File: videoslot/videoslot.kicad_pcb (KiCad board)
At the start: 2 copper layers, 100 x 24 mm, 11 parts, among them CN203 CN451/203, CN207 CN452/207, P1 VA2000, U1 74LVC8T245, U2 74LVC8T245

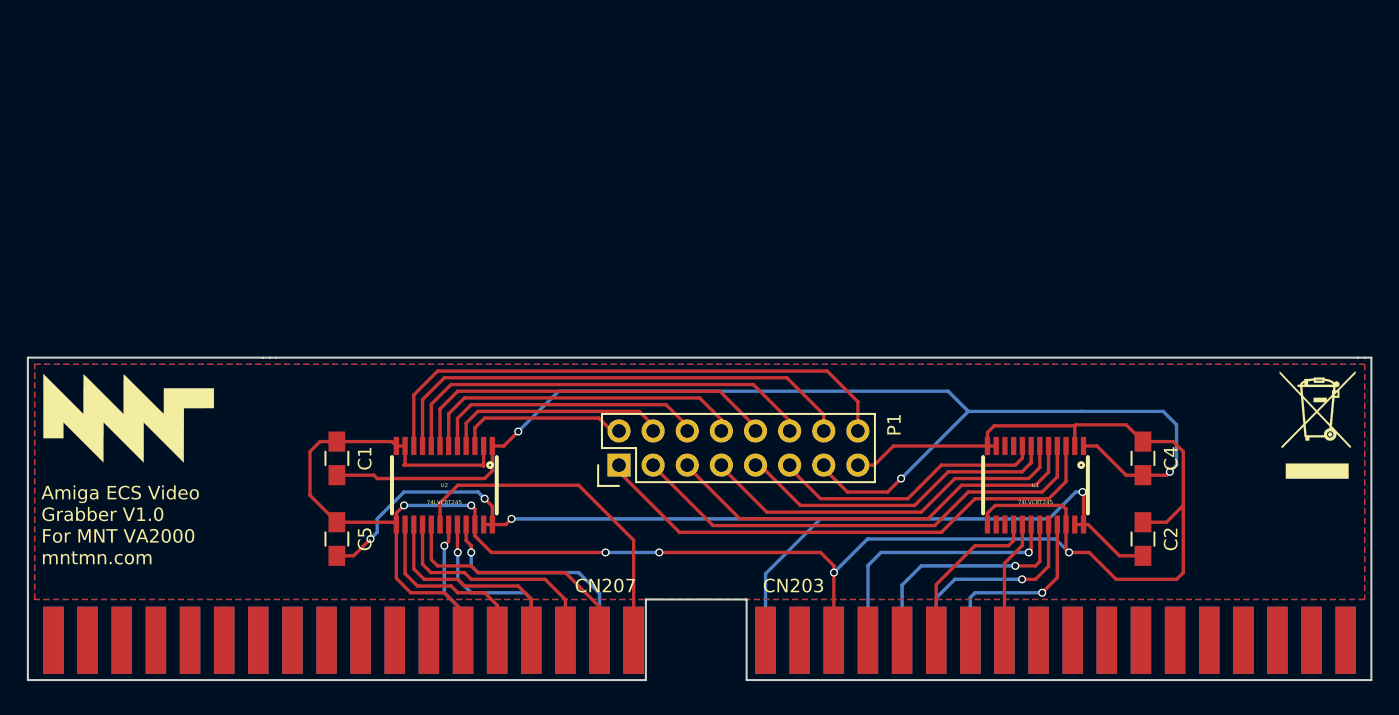
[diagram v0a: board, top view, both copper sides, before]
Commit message: VA2000CX corrections for PCB batch 1
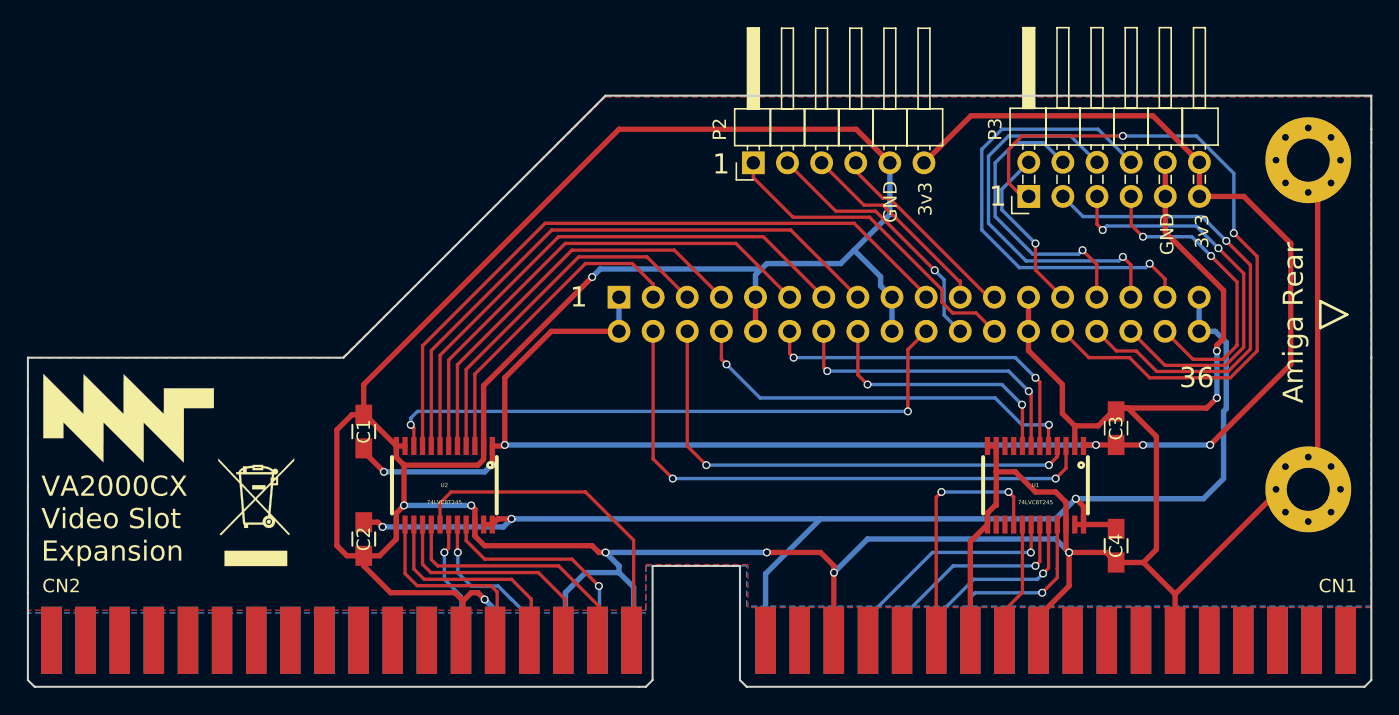
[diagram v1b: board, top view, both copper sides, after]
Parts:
- removed C5: C, Capacitors_SMD:C_0805_HandSoldering
- removed CN203: CN451/203, mntamiga:CN451
- removed CN207: CN452/207, mntamiga:CN452
- added ?: , Mounting_Holes:MountingHole_3.2mm_M3_Pad_Via, F.Cu at (231.8, 107.8)
- added ?: , Mounting_Holes:MountingHole_3.2mm_M3_Pad_Via, F.Cu at (231.8, 83.3)
- added C3: C, Capacitors_SMD:C_0805_HandSoldering, F.Cu at (217.5, 103.2)
- added CN1: CN451/203, mntamiga:CN451, F.Cu at (213.0, 116.5)
- added CN2: CN452/207, mntamiga:CN452, F.Cu at (159.8, 116.5)
- added P2: PMOD1, Pin_Headers:Pin_Header_Angled_1x06_Pitch2.54mm, F.Cu at (190.5, 83.5)
- added P3: PMOD2, Pin_Headers:Pin_Header_Angled_2x06_Pitch2.54mm, F.Cu at (211.0, 86.0)
- P1: value VA2000 -> UPLINK; footprint Pin_Headers:Pin_Header_Straight_2x08 -> Pin_Headers:Pin_Header_Straight_2x18_Pitch2.54mm; moved to B.Cu
- moved G*** 79.3 mm to (153.5, 109.5)
- moved C2 58.0 mm to (161.5, 111.5), turned to 90 degrees
- moved P1 12.5 mm to (180.5, 93.5), turned to 270 degrees
- moved C4 6.80 mm to (217.5, 112.0), turned to 90 degrees
- moved C1 2.83 mm to (161.5, 103.5)
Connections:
- C1 pad 2: Net-(C1-Pad2) -> +3V3
- C2 pad 2: Net-(C2-Pad2) -> +5V
- C4 pad 2: Net-(C1-Pad2) -> +5V
- P1 pad 1: Net-(P1-Pad1) -> +3V3
- P1 pad 10: Net-(P1-Pad10) -> GND
- P1 pad 11: Net-(P1-Pad11) -> /r0
- P1 pad 12: Net-(P1-Pad12) -> /r3
- P1 pad 13: Net-(C1-Pad2) -> /r2
- P1 pad 14: Net-(P1-Pad14) -> /HS
- P1 pad 15: GND -> /g0
- P1 pad 16: Net-(P1-Pad16) -> /VS
- P1 pad 2: Net-(P1-Pad2) -> +3V3
- P1 pad 3: Net-(P1-Pad3) -> /r1
- P1 pad 4: Net-(P1-Pad4) -> /b0
- P1 pad 5: Net-(P1-Pad5) -> /g1
- P1 pad 6: Net-(P1-Pad6) -> /b3
- P1 pad 7: Net-(P1-Pad7) -> /b2
- P1 pad 8: Net-(P1-Pad8) -> /g3
- P1 pad 9: Net-(P1-Pad9) -> GND
- U1 pad 1: Net-(C1-Pad2) -> +3V3
- U1 pad 23: Net-(C2-Pad2) -> +5V
- U1 pad 24: Net-(C2-Pad2) -> +5V
- U1 pad 3: Net-(P1-Pad1) -> /b0
- U1 pad 4: Net-(P1-Pad3) -> /b3
- U1 pad 5: Net-(P1-Pad5) -> /g3
- U1 pad 6: Net-(P1-Pad7) -> /r3
- U1 pad 7: Net-(P1-Pad9) -> /HS
- U1 pad 8: Net-(P1-Pad11) -> /VS
- U2 pad 1: Net-(C1-Pad2) -> +3V3
- U2 pad 10: Net-(P1-Pad16) -> /b1
- U2 pad 23: Net-(C2-Pad2) -> +5V
- U2 pad 24: Net-(C2-Pad2) -> +5V
- U2 pad 3: Net-(P1-Pad2) -> /r1
- U2 pad 4: Net-(P1-Pad4) -> /g1
- U2 pad 5: Net-(P1-Pad6) -> /b2
- U2 pad 6: Net-(P1-Pad8) -> /r0
- U2 pad 7: Net-(P1-Pad10) -> /r2
- U2 pad 8: Net-(P1-Pad12) -> /g0
- U2 pad 9: Net-(P1-Pad14) -> /g2
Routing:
- net GND: track 161.8 -> 375.2 mm, vias 6 -> 10
- net +3V3: track 0.00 -> 135.6 mm, vias 0 -> 6
- net +5V: track 0.00 -> 100.2 mm, vias 0 -> 3
- net Net-(C1-Pad2): track 92.8 -> 0.00 mm, vias 3 -> 0
- net Net-(C2-Pad2): track 81.7 -> 0.00 mm, vias 4 -> 0
- net Net-(P1-Pad28): track 0.00 -> 53.4 mm, vias 0 -> 2
- net /g2: track 0.00 -> 51.1 mm
- net /b1: track 0.00 -> 45.9 mm, vias 0 -> 2
- net /g0: track 0.00 -> 44.6 mm
- net /b0: track 0.00 -> 42.8 mm, vias 0 -> 2
- net /r2: track 0.00 -> 40.8 mm
- net Net-(P1-Pad16): track 40.7 -> 0.00 mm
- net Net-(P1-Pad1): track 39.9 -> 0.00 mm
- net /b3: track 0.00 -> 37.7 mm, vias 0 -> 2
- net /r0: track 0.00 -> 37.0 mm
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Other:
- board size 100 x 24 mm -> 100 x 44 mm
- net class Power added: clearance 0.2, trace_width 0.4, via_dia 0.6, via_drill 0.4
- board text added: "1"
- board text added: "36"
- board text added: "3v3"
- board text added: "Amiga Rear"
- board text added: "GND"
- board text added: "VA2000CX Video Slot Expansion"
- board text removed: "Amiga ECS Video Grabber V1.0 For MNT VA2000 mntmn.com"

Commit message: WIP 1.5b firmware, gfx drivers; mntmode, va2000cx initial commits
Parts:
- moved G*** 0.36 mm to (153.2, 109.3)
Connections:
- CN1 pad 35: +5V -> Net-(CN1-Pad35)
- CN1 pad 6: Net-(CN1-Pad6) -> +5V
- CN1 pad 8: Net-(CN1-Pad8) -> +5V
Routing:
- net GND: track 375.2 -> 314.4 mm, vias 10 -> 5
- net +5V: track 100.2 -> 110.8 mm
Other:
- board text added: "5v"
- board text added: "R2"
- board text added: "b0"
- board text added: "b1"
- board text added: "b2"
- board text added: "b3"
- board text added: "g0"
- board text added: "g1"
- board text added: "g2"
- board text added: "g3"
- board text added: "hs"
- board text added: "r0"
- board text added: "r1"
- board text added: "r2"
- board text added: "r3"
- board text added: "vs"
